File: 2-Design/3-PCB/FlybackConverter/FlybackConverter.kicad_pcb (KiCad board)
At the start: 2 copper layers, 7 parts, among them U1 TL431D

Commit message: i am trying to handle layout
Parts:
- added CA1: C, Capacitor_SMD:C_0805_2012Metric_Pad1.18x1.45mm_HandSolder, F.Cu at (75.2, 76.7)
- added CF1: C, Capacitor_SMD:C_0805_2012Metric_Pad1.18x1.45mm_HandSolder, F.Cu at (78.7, 74.9)
- added CIN1: C, Capacitor_SMD:CP_Elec_10x10.5, F.Cu at (36.6, 61.0)
- added CIN2: C, Capacitor_SMD:CP_Elec_10x10.5, F.Cu at (36.3, 49.3)
- added CIN3: C, Capacitor_SMD:CP_Elec_10x10.5, F.Cu at (36.8, 73.2)
- added CIN4: C, Capacitor_SMD:CP_Elec_10x10.5, F.Cu at (36.3, 37.6)
- added COUT1: C, Capacitor_SMD:CP_Elec_10x10.5, F.Cu at (173.7, 25.9)
- added COUT2: C, Capacitor_SMD:CP_Elec_10x10.5, F.Cu at (173.7, 62.0)
- added COUT3: C, Capacitor_SMD:CP_Elec_10x10.5, F.Cu at (173.7, 49.8)
- added COUT4: C, Capacitor_SMD:CP_Elec_10x10.5, F.Cu at (173.7, 37.8)
- added CP1: C, Capacitor_SMD:C_0805_2012Metric_Pad1.18x1.45mm_HandSolder, F.Cu at (118.9, 63.5)
- added CS1: C, Capacitor_SMD:C_0805_2012Metric_Pad1.18x1.45mm_HandSolder, F.Cu at (86.9, 68.1)
- added CSnubber1: C, Capacitor_SMD:C_2220_5650Metric_Pad1.97x5.40mm_HandSolder, F.Cu at (76.1, 41.6)
- added CT1: C, Capacitor_SMD:C_0805_2012Metric_Pad1.18x1.45mm_HandSolder, F.Cu at (82.3, 67.1)
- added CVCC1: C, Capacitor_SMD:C_0805_2012Metric_Pad1.18x1.45mm_HandSolder, F.Cu at (76.2, 61.0)
- added CVCC2: C, Capacitor_SMD:CP_Elec_8x5.4, F.Cu at (58.7, 61.2)
- added CVREF1: C, Capacitor_SMD:C_0805_2012Metric_Pad1.18x1.45mm_HandSolder, F.Cu at (67.3, 65.5)
- added CZ1: C, Capacitor_SMD:C_0805_2012Metric_Pad1.18x1.45mm_HandSolder, F.Cu at (123.2, 65.0)
- added DC1: DZ2S100X0L, Diode_SMD:D_SOD-523, F.Cu at (134.6, 61.5)
- added DSnubber1: MBRA340, Diode_SMD:D_SMA, F.Cu at (83.1, 38.6)
- added INPUT1: Conn_01x02_Female, TerminalBlock_Phoenix:TerminalBlock_Phoenix_MKDS-1,5-2-5.08_1x02_P5.08mm_Horizontal, F.Cu at (37.8, 24.6)
- added OUTPUT1: Conn_01x02_Female, TerminalBlock_Phoenix:TerminalBlock_Phoenix_MKDS-1,5-2-5.08_1x02_P5.08mm_Horizontal, F.Cu at (172.2, 74.4)
- added RA1: R, Resistor_SMD:R_0805_2012Metric_Pad1.20x1.40mm_HandSolder, F.Cu at (75.2, 72.9)
- added RAC1: R, Resistor_SMD:R_0805_2012Metric_Pad1.20x1.40mm_HandSolder, F.Cu at (130.8, 67.8)
- added RB1: R, Resistor_SMD:R_0805_2012Metric_Pad1.20x1.40mm_HandSolder, F.Cu at (80.0, 78.5)
- added RC1: R, Resistor_SMD:R_0805_2012Metric_Pad1.20x1.40mm_HandSolder, F.Cu at (85.1, 75.9)
- added RCS1: R, Resistor_SMD:R_2010_5025Metric_Pad1.40x2.65mm_HandSolder, F.Cu at (110.2, 73.7)
- added RE1: R, Resistor_SMD:R_0805_2012Metric_Pad1.20x1.40mm_HandSolder, F.Cu at (135.4, 66.8)
- added RF1: R, Resistor_SMD:R_0805_2012Metric_Pad1.20x1.40mm_HandSolder, F.Cu at (116.1, 78.0)
- added RG1: R, Resistor_SMD:R_0805_2012Metric_Pad1.20x1.40mm_HandSolder, F.Cu at (80.8, 60.7)
- added RI1: R, Resistor_SMD:R_0805_2012Metric_Pad1.20x1.40mm_HandSolder, F.Cu at (130.6, 63.5)
- added RJ1: R, Resistor_SMD:R_0805_2012Metric_Pad1.20x1.40mm_HandSolder, F.Cu at (118.6, 73.4)
- added RK1: R, Resistor_SMD:R_0805_2012Metric_Pad1.20x1.40mm_HandSolder, F.Cu at (127.0, 64.3)
- added RP1: R, Resistor_SMD:R_0805_2012Metric_Pad1.20x1.40mm_HandSolder, F.Cu at (67.3, 70.1)
- added RS1: R, Resistor_SMD:R_0805_2012Metric_Pad1.20x1.40mm_HandSolder, F.Cu at (83.8, 71.6)
- added RS2: R, Resistor_SMD:R_0805_2012Metric_Pad1.20x1.40mm_HandSolder, F.Cu at (88.1, 58.9)
- added RSnubber1: R, Resistor_SMD:R_2010_5025Metric_Pad1.40x2.65mm_HandSolder, F.Cu at (76.1, 35.3)
- added RT1: 10, Resistor_SMD:R_0805_2012Metric_Pad1.20x1.40mm_HandSolder, F.Cu at (87.9, 63.8)
- added RZ1: R, Resistor_SMD:R_0805_2012Metric_Pad1.20x1.40mm_HandSolder, F.Cu at (118.9, 66.8)
- added TVS1: MBRA340, Diode_SMD:D_SMA, F.Cu at (51.3, 61.7)
- added TestPointA1: Conn_01x01_Female, TestPoint:TestPoint_Pad_2.5x2.5mm, F.Cu at (118.6, 58.2)
- added TestPointB1: Conn_01x01_Female, TestPoint:TestPoint_Pad_2.5x2.5mm, F.Cu at (90.4, 78.0)
- added TestPointC1: Conn_01x01_Female, TestPoint:TestPoint_Pad_2.5x2.5mm, F.Cu at (69.3, 77.0)
- added Vo'1: Conn_01x01_Female, TestPoint:TestPoint_Pad_2.5x2.5mm, F.Cu at (132.3, 72.4)
- added Vo1: Conn_01x01_Female, TestPoint:TestPoint_Pad_2.5x2.5mm, F.Cu at (134.6, 36.1)
- TR1: footprint Transformer_THT:Transformer_Breve_TEZ-35x42 -> kutup:sevgi-kafkasi
- moved TVS_SUBSTITUTE1 185.7 mm to (53.7, -87.4)
- moved TR1 57.0 mm to (92.7, 50.0)
- moved MOSFET1 38.3 mm to (97.5, 74.3), turned to -90 degrees
- moved FLYBACK_DIODE_SUBSTITUTE1 37.1 mm to (131.3, 29.5), turned to 180 degrees
- moved PWMController1 22.3 mm to (77.7, 67.1), turned to 90 degrees
- moved OPTO1 18.9 mm to (106.9, 64.3), turned to 180 degrees
- moved U1 1.80 mm to (125.5, 73.2)
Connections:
- PWMController1 pad 7: Net-(TVS_SUBSTITUTE1-Pad1) -> Net-(CVCC1-Pad2)
- TVS_SUBSTITUTE1 pad 1: Net-(TVS_SUBSTITUTE1-Pad1) -> unconnected-(TVS_SUBSTITUTE1-Pad1)
- TVS_SUBSTITUTE1 pad 2: Net-(MOSFET1-Pad1) -> unconnected-(TVS_SUBSTITUTE1-Pad2)
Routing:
- net Net-(CVCC1-Pad2): track 0.00 -> 29.9 mm
- net Net-(CIN1-Pad1): track 0.00 -> 28.6 mm
- net Net-(CF1-Pad1): track 0.00 -> 23.3 mm
- net Net-(DSnubber1-Pad2): track 0.00 -> 17.4 mm
- net Net-(CA1-Pad2): track 0.00 -> 13.3 mm
- net Net-(CS1-Pad1): track 0.00 -> 13.0 mm
- net Net-(CVREF1-Pad1): track 0.00 -> 12.0 mm
- net Net-(CA1-Pad1): track 0.00 -> 11.7 mm
- net Net-(OPTO1-Pad3): track 0.00 -> 11.2 mm
- net Net-(CSnubber1-Pad2): track 0.00 -> 11.2 mm
- net Net-(PWMController1-Pad6): track 0.00 -> 4.46 mm
- net Net-(CS1-Pad2): track 0.00 -> 3.97 mm

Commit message: first tentavie layout
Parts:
- moved CVCC2 45.8 mm to (103.1, 72.4), turned to 90 degrees
- moved TVS1 44.8 mm to (93.5, 77.0), turned to 180 degrees
- moved RCS1 34.0 mm to (84.8, 51.1)
- moved MOSFET1 30.6 mm to (77.9, 50.8), turned to 0 degrees
- moved CVREF1 27.3 mm to (94.5, 63.5), turned to 0 degrees
- moved RB1 24.4 mm to (93.5, 58.2)
- moved RC1 23.9 mm to (102.1, 59.2)
- moved TestPointB1 22.0 mm to (110.0, 67.8)
- moved RP1 19.5 mm to (86.3, 74.4), turned to 180 degrees
- moved CVCC1 18.7 mm to (93.7, 67.6), turned to 90 degrees
- moved DC1 16.1 mm to (133.3, 77.5), turned to 0 degrees
- moved RS2 14.7 mm to (73.7, 61.2), turned to 90 degrees
- moved CA1 11.8 mm to (78.0, 65.3), turned to 90 degrees
- moved TestPointC1 11.3 mm to (71.1, 65.8)
- moved RE1 10.2 mm to (137.7, 76.7), turned to 0 degrees
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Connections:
- COUT1 pad 2: Net-(COUT1-Pad2) -> GND1
- COUT2 pad 2: Net-(COUT1-Pad2) -> GND1
- COUT3 pad 2: Net-(COUT1-Pad2) -> GND1
- COUT4 pad 2: Net-(COUT1-Pad2) -> GND1
- OUTPUT1 pad 2: Net-(COUT1-Pad2) -> GND1
- TR1 pad 6: Net-(COUT1-Pad2) -> GND1
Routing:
- net Net-(CIN1-Pad1): track 28.6 -> 121.8 mm
- net Net-(CA1-Pad1): track 11.7 -> 102.5 mm
- net Net-(COUT1-Pad1): track 0.00 -> 49.8 mm
- net GND1: track 0.00 -> 48.8 mm
- net Net-(CP1-Pad1): track 0.00 -> 29.1 mm
- net Net-(DC1-Pad1): track 0.00 -> 28.5 mm
- net Net-(MOSFET1-Pad1): track 0.00 -> 27.6 mm
- net Net-(CP1-Pad2): track 0.00 -> 24.2 mm
- net Net-(CF1-Pad1): track 23.3 -> 44.5 mm
- net Net-(OPTO1-Pad1): track 0.00 -> 19.6 mm
- net Net-(DSnubber1-Pad2): track 17.4 -> 34.8 mm
- net Net-(MOSFET1-Pad4): track 0.00 -> 13.9 mm
- net Net-(OPTO1-Pad3): track 11.2 -> 22.1 mm
- net Net-(FLYBACK_DIODE_SUBSTITUTE1-Pad2): track 0.00 -> 9.91 mm
- net Net-(CVREF1-Pad1): track 12.0 -> 21.7 mm
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- added copper zone on F.Cu, net GND1

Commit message: something new?
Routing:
- net Net-(COUT1-Pad1): track 49.8 -> 136.2 mm
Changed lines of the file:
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@@
   (segment (start 86.646 39.402) (end 87.122 39.878) (width 1) (layer "F.Cu") (net 5))
   (segment (start 86.868 42.926) (end 86.868 36.83) (width 1) (layer "F.Cu") (net 5))
-  (segment (start 73.7025 31.7075) (end 74.93 30.48) (width 1) (layer "F.Cu") (net 6))
+  (segment (start 73.7025 31.7075) (end 74.93 30.48) (width 2.3) (layer "F.Cu") (net 6))
   (segment (start 32.55413 41.61387) (end 32.122 42.046) (width 1) (layer "F.Cu") (net 6))
-  (segment (start 74.93 30.48) (end 88.392 30.48) (width 1) (layer "F.Cu") (net 6))
+  (segment (start 74.93 30.48) (end 88.392 30.48) (width 2.3) (layer "F.Cu") (net 6))
   (segment (start 32.376 72.898) (end 32.63 73.152) (width 1) (layer "F.Cu") (net 6))
-  (segment (start 32.766 24.638) (end 32.766 36.948) (width 1) (layer "F.Cu") (net 6))
+  (segment (start 32.766 24.638) (end 32.766 36.948) (width 3) (layer "F.Cu") (net 6))
   (segment (start 73.7025 41.37637) (end 73.465 41.61387) (width 1) (layer "F.Cu") (net 6))
-  (segment (start 32.376 60.96) (end 32.376 49.53) (width 1) (layer "F.Cu") (net 6))
-  (segment (start 32.122 42.046) (end 32.122 49.276) (width 1) (layer "F.Cu") (net 6))
+  (segment (start 32.376 60.96) (end 32.376 49.53) (width 3) (layer "F.Cu") (net 6))
+  (segment (start 32.122 42.046) (end 32.122 49.276) (width 3) (layer "F.Cu") (net 6))
   (segment (start 32.766 36.948) (end 32.122 37.592) (width 1) (layer "F.Cu") (net 6))
   (segment (start 32.376 49.53) (end 32.122 49.276) (width 1) (layer "F.Cu") (net 6))
-  (segment (start 73.7025 35.26387) (end 73.7025 41.37637) (width 1) (layer "F.Cu") (net 6))
-  (segment (start 32.122 37.592) (end 32.122 42.046) (width 1) (layer "F.Cu") (net 6))
-  (segment (start 73.7025 35.26387) (end 73.7025 31.7075) (width 1) (layer "F.Cu") (net 6))
-  (segment (start 73.465 41.61387) (end 32.55413 41.61387) (width 1) (layer "F.Cu") (net 6))
-  (segment (start 32.376 60.96) (end 32.376 72.898) (width 1) (layer "F.Cu") (net 6))
-  (segment (start 88.392 30.48) (end 92.71 34.798) (width 1) (layer "F.Cu") (net 6))
+  (segment (start 73.7025 35.26387) (end 73.7025 41.37637) (width 2.3) (layer "F.Cu") (net 6))
+  (segment (start 32.122 37.592) (end 32.122 42.046) (width 3) (layer "F.Cu") (net 6))
+  (segment (start 73.7025 35.26387) (end 73.7025 31.7075) (width 2.3) (layer "F.Cu") (net 6))
+  (segment (start 73.465 41.61387) (end 32.55413 41.61387) (width 3) (layer "F.Cu") (net 6))
+  (segment (start 32.376 60.96) (end 32.376 72.898) (width 3) (layer "F.Cu") (net 6))
+  (segment (start 88.392 30.48) (end 92.71 34.798) (width 2.3) (layer "F.Cu") (net 6))
   (segment (start 113.919 64.135) (end 108.5975 64.135) (width 1) (layer "F.Cu") (net 7))
   (segment (start 115.062 65.278) (end 113.919 64.135) (width 1) (layer "F.Cu") (net 7))
@@
   (segment (start 81.788 67.564) (end 81.573 67.779) (width 1) (layer "F.Cu") (net 15))
   (segment (start 177.292 62.62) (end 177.936 61.976) (width 1) (layer "F.Cu") (net 16))
-  (segment (start 177.936 49.784) (end 177.936 37.846) (width 1) (layer "F.Cu") (net 16))
-  (segment (start 177.292 74.422) (end 177.292 62.62) (width 1) (layer "F.Cu") (net 16))
-  (segment (start 177.936 25.908) (end 177.936 37.846) (width 1) (layer "F.Cu") (net 16))
-  (segment (start 177.936 61.976) (end 177.936 49.784) (width 1) (layer "F.Cu") (net 16))
+  (segment (start 177.936 49.784) (end 177.936 37.846) (width 3) (layer "F.Cu") (net 16))
+  (segment (start 177.292 74.422) (end 177.292 62.62) (width 3) (layer "F.Cu") (net 16))
+  (segment (start 177.936 25.908) (end 177.936 37.846) (width 3) (layer "F.Cu") (net 16))
+  (segment (start 177.936 61.976) (end 177.936 49.784) (width 3) (layer "F.Cu") (net 16))
   (segment (start 83.885 70.9095) (end 84.6035 71.628) (width 1) (layer "F.Cu") (net 17))
   (segment (start 87.662 71.628) (end 84.6035 71.628) (width 1) (layer "F.Cu") (net 17))
@@
   (segment (start 132.112 69.374) (end 132.112 67.818) (width 1) (layer "F.Cu") (net 19))
   (segment (start 134.718 35.97) (end 134.62 36.068) (width 1) (layer "F.Cu") (net 20))
-  (segment (start 136.144 60.198) (end 136.144 65.786) (width 1) (layer "F.Cu") (net 20))
-  (segment (start 134.718 29.464) (end 134.718 35.97) (width 1) (layer "F.Cu") (net 20))
+  (segment (start 137.922 61.976) (end 136.144 60.198) (width 3) (layer "F.Cu") (net 20))
+  (segment (start 169.536 61.976) (end 137.922 61.976) (width 3) (layer "F.Cu") (net 20))
+  (segment (start 134.718 29.464) (end 134.718 35.97) (width 3) (layer "F.Cu") (net 20))
   (segment (start 136.652 70.358) (end 134.112 67.818) (width 1) (layer "F.Cu") (net 20))
-  (segment (start 134.62 58.674) (end 136.144 60.198) (width 1) (layer "F.Cu") (net 20))
-  (segment (start 134.62 36.068) (end 134.62 58.674) (width 1) (layer "F.Cu") (net 20))
-  (segment (start 136.652 76.708) (end 136.652 70.358) (width 1) (layer "F.Cu") (net 20))
-  (segment (start 136.144 65.786) (end 134.112 67.818) (width 1) (layer "F.Cu") (net 20))
+  (segment (start 169.536 49.784) (end 169.536 37.846) (width 3) (layer "F.Cu") (net 20))
+  (segment (start 134.62 58.674) (end 136.144 60.198) (width 3) (layer "F.Cu") (net 20))
+  (segment (start 136.144 60.198) (end 136.144 68.834) (width 3) (layer "F.Cu") (net 20))
+  (segment (start 169.536 25.908) (end 169.536 37.846) (width 3) (layer "F.Cu") (net 20))
+  (segment (start 169.926 61.586) (end 169.536 61.976) (width 0.25) (layer "F.Cu") (net 20))
+  (segment (start 134.62 36.068) (end 134.62 58.674) (width 3) (layer "F.Cu") (net 20))
+  (segment (start 169.926 47.498) (end 169.926 61.586) (width 3) (layer "F.Cu") (net 20))
+  (segment (start 169.536 61.976) (end 172.212 64.652) (width 3) (layer "F.Cu") (net 20))
+  (segment (start 172.212 64.652) (end 172.212 74.422) (width 3) (layer "F.Cu") (net 20))
+  (segment (start 136.652 76.708) (end 136.652 70.358) (width 1.3) (layer "F.Cu") (net 20))
   (segment (start 126.238 62.23) (end 132.826 62.23) (width 1) (layer "F.Cu") (net 21))
   (segment (start 125.984 70.866) (end 126.365 71.247) (width 1) (layer "F.Cu") (net 21))

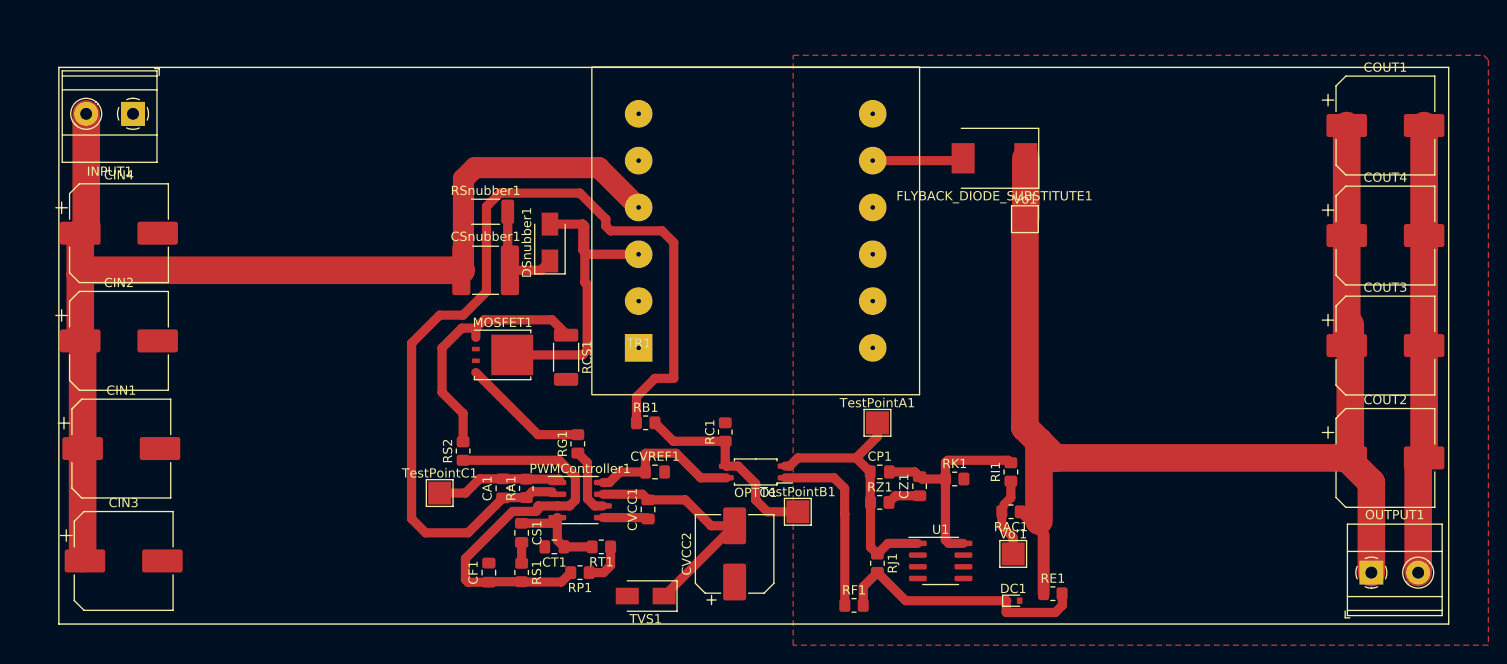
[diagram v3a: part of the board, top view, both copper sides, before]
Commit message: added vias
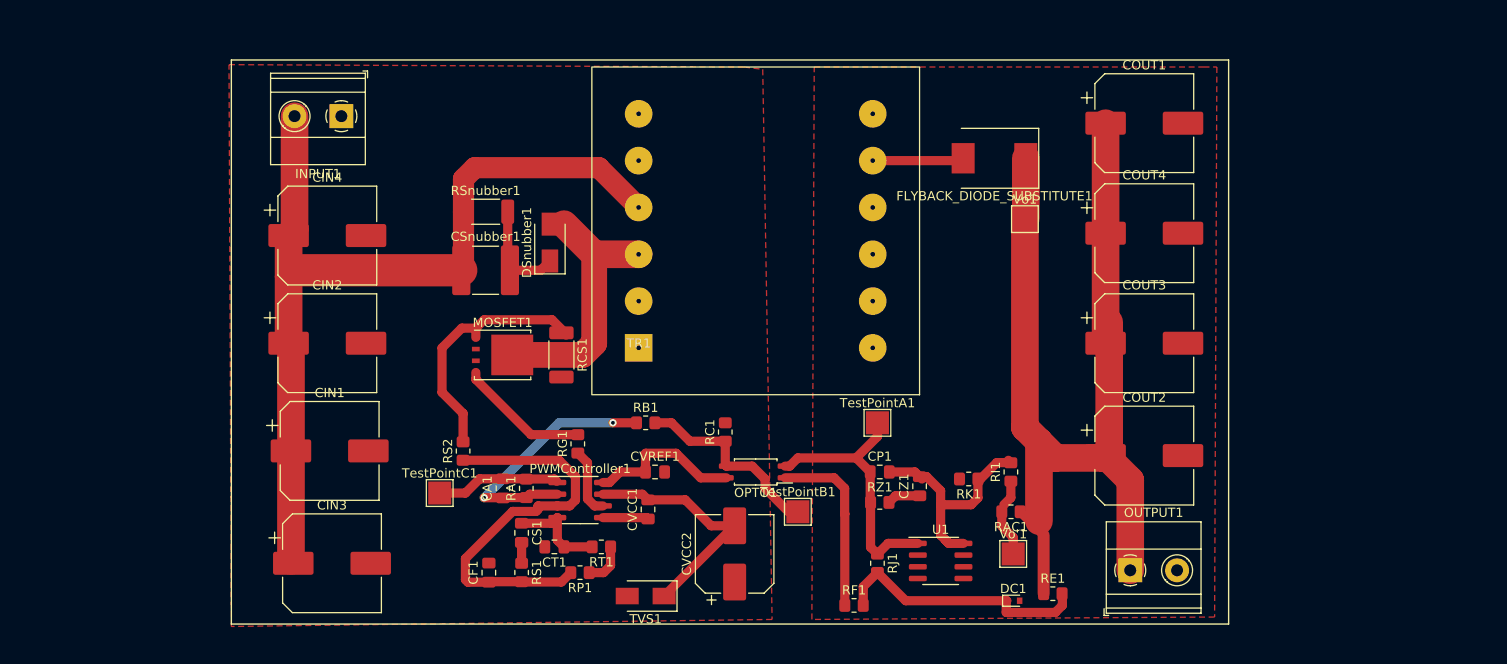
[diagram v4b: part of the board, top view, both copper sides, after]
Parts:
- moved COUT1 26.2 mm to (147.6, 25.7)
- moved COUT2 26.2 mm to (147.6, 61.7)
- moved COUT3 26.2 mm to (147.6, 49.5)
- moved COUT4 26.2 mm to (147.6, 37.6)
- moved OUTPUT1 26.2 mm to (146.1, 74.2)
- moved CIN1 22.6 mm to (59.2, 61.2)
- moved CIN3 22.6 mm to (59.4, 73.4)
- moved INPUT1 22.6 mm to (60.5, 24.9)
- moved CIN2 22.6 mm to (58.9, 49.5)
- moved CIN4 22.6 mm to (58.9, 37.8)
- moved RK1 1.52 mm to (128.5, 64.3), turned to 180 degrees
- moved RCS1 0.57 mm to (84.3, 50.8)
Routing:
- net Net-(CA1-Pad1): track 102.5 -> 28.0 mm, vias 0 -> 2
- net GND1: track 48.8 -> 0.91 mm
- net Net-(COUT1-Pad1): track 136.2 -> 110.1 mm
- net Net-(CIN1-Pad1): track 121.8 -> 99.3 mm
- net Net-(DSnubber1-Pad2): track 34.8 -> 30.1 mm
- net Net-(CP1-Pad2): track 24.2 -> 26.1 mm
- added copper zone on F.Cu, net GND
